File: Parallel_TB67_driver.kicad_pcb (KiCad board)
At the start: 2 copper layers, 7 parts, among them J1 Vin, J2 Vout, J3 Driver_pinout, J4 MotorA, J5 MotorB, U1 Driver Module

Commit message: PCB completed
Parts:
- moved J3 18.1 mm to (159.4, 79.5)
- moved C1 17.7 mm to (148.9, 111.3)
- moved J2 17.7 mm to (138.8, 81.5)
- moved J5 17.7 mm to (138.8, 102.4)
- moved J1 17.7 mm to (138.8, 112.8)
- moved J4 17.7 mm to (138.8, 92.0)
- moved U1 17.7 mm to (152.7, 96.8)
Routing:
- net /IN_B2: track 0.00 -> 28.4 mm, vias 0 -> 1
- net /IN_B1: track 0.00 -> 25.2 mm, vias 0 -> 1
- net /VREF: track 0.00 -> 21.0 mm
- net /IN_A2: track 0.00 -> 18.1 mm
- net /IN_A1: track 0.00 -> 15.2 mm
- net GND: vias 0 -> 11
- added copper zone on B.Cu, net /OUT_A1
- added copper zone on B.Cu, net /OUT_A2
- added copper zone on B.Cu, net /OUT_B1
- added copper zone on B.Cu, net /OUT_B2
- added copper zone on B.Cu, net /VM
- added copper zone on B.Cu, net GND
- added copper zone on F.Cu, net GND
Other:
- board outline added: 26.2 x 42.2 mm

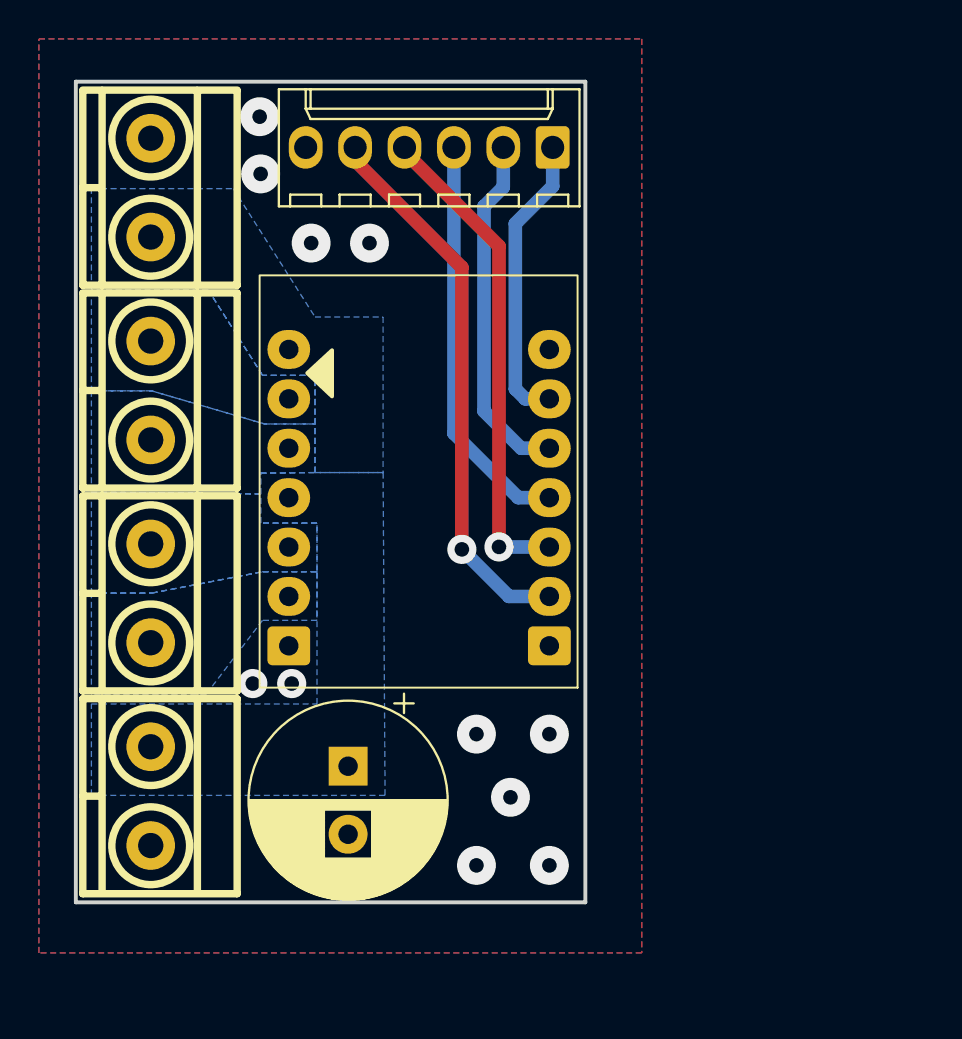
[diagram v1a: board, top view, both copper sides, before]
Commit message: Fixed bottom layer molex pins connection
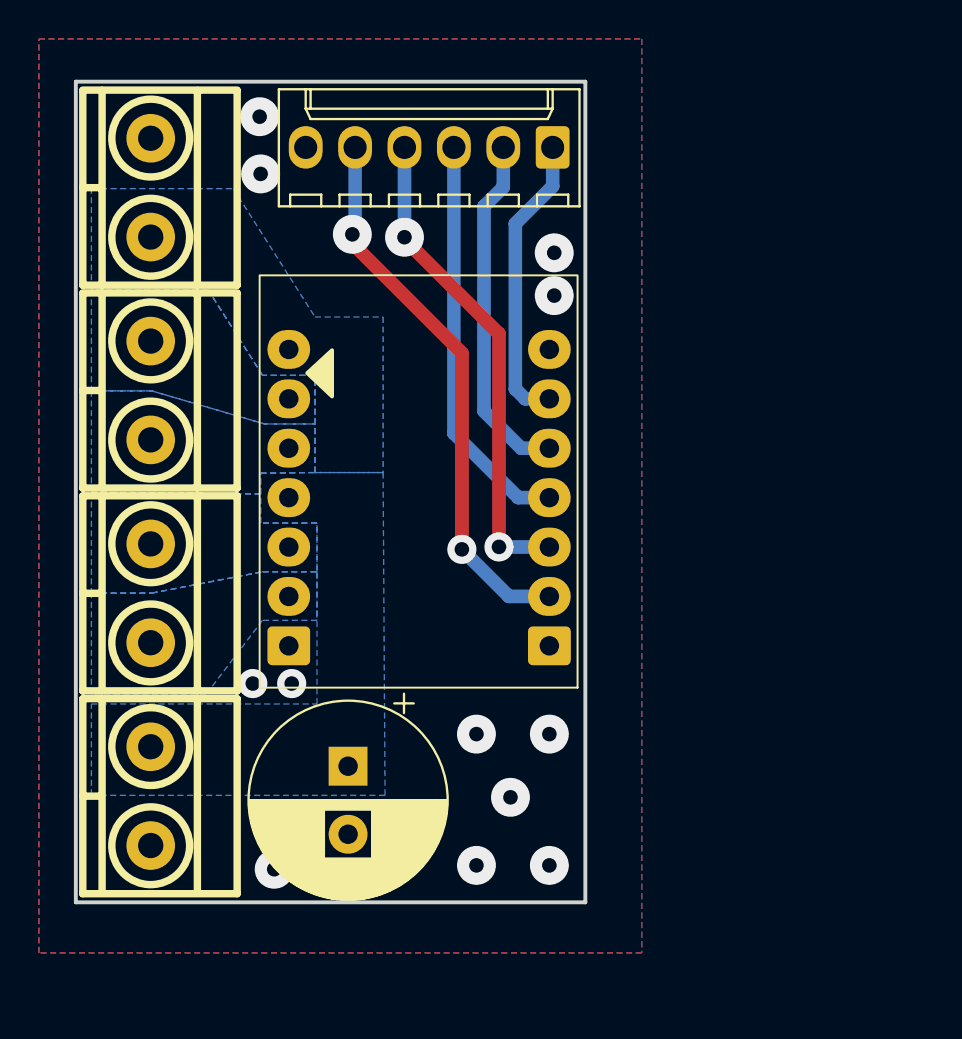
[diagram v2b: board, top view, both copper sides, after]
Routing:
- net /IN_B2: track 28.4 -> 28.6 mm, vias 1 -> 2
- net GND: vias 11 -> 13
- net /IN_B1: vias 1 -> 2
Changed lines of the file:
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@@
 	)
 	(via
-		(at 150 84.4)
+		(at 159.5 84.9)
 		(size 2)
 		(drill 0.75)
@@
 	)
 	(via
-		(at 147 84.4)
+		(at 159.5 87.1)
 		(size 2)
 		(drill 0.75)
@@
 	(via
 		(at 159.25 109.65)
+		(size 2)
+		(drill 0.75)
+		(layers "F.Cu" "B.Cu")
+		(free yes)
+		(net 1)
+	)
+	(via
+		(at 145.1 116.6)
 		(size 2)
 		(drill 0.75)
@@
 	)
 	(via
+		(at 145.1 114.3)
+		(size 2)
+		(drill 0.75)
+		(layers "F.Cu" "B.Cu")
+		(free yes)
+		(net 1)
+	)
+	(via
 		(at 144.352118 77.9)
 		(size 2)
@@
 	)
 	(segment
-		(start 149.26 80.16)
-		(end 149.26 79.48)
+		(start 149.11879 83.950676)
+		(end 149.11879 84.41879)
 		(width 0.7)
 		(layer "F.Cu")
@@
 	)
 	(segment
-		(start 154.75 85.65)
-		(end 149.26 80.16)
+		(start 149.11879 84.41879)
+		(end 154.75 90.05)
 		(width 0.7)
 		(layer "F.Cu")
@@
 	)
 	(segment
-		(start 154.75 100.15)
-		(end 154.75 85.65)
+		(start 154.75 90.05)
+		(end 154.75 100.15)
 		(width 0.7)
 		(layer "F.Cu")
@@
 		(net 3)
 	)
+	(via
+		(at 149.11879 83.950676)
+		(size 2)
+		(drill 0.75)
+		(layers "F.Cu" "B.Cu")
+		(net 3)
+	)
+	(segment
+		(start 149.26 83.809466)
+		(end 149.26 79.48)
+		(width 0.7)
+		(layer "B.Cu")
+		(net 3)
+	)
 	(segment
 		(start 157.17 102.57)
 		(end 154.75 100.15)
+		(width 0.7)
+		(layer "B.Cu")
+		(net 3)
+	)
+	(segment
+		(start 149.11879 83.950676)
+		(end 149.26 83.809466)
 		(width 0.7)
 		(layer "B.Cu")
@@
 	)
 	(segment
-		(start 156.658203 84.558203)
-		(end 151.8 79.7)
+		(start 151.8 84.1)
+		(end 151.8 84.2)
 		(width 0.7)
 		(layer "F.Cu")
@@
 	)
 	(segment
-		(start 151.8 79.7)
-		(end 151.8 79.48)
+		(start 156.658203 89.058203)
+		(end 156.658203 100.023436)
 		(width 0.7)
 		(layer "F.Cu")
@@
 	)
 	(segment
-		(start 156.658203 100.023436)
-		(end 156.658203 84.558203)
+		(start 151.8 84.2)
+		(end 156.658203 89.058203)
 		(width 0.7)
 		(layer "F.Cu")
@@
 		(net 4)
 	)
+	(via
+		(at 151.8 84.1)
+		(size 2)
+		(drill 0.75)
+		(layers "F.Cu" "B.Cu")
+		(net 4)
+	)
 	(segment
 		(start 159.25 100.03)
@@
 		(width 0.7)
 		(layer "B.Cu")
+		(net 4)
+	)
+	(segment
+		(start 151.8 84.1)
+		(end 151.8 79.48)
+		(width 0.7)
+		(layer "B.Cu")
